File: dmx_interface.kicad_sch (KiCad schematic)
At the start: 12 parts, among them J1 NC3MAAH, J2 NC3FAAH, U1 ST485E

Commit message: mcu pinouts and extras
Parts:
- *C3, *C4: footprint (none) -> Capacitor_SMD:C_0603_1608Metric_Pad1.08x0.95mm_HandSolder
- JP1: footprint (none) -> Jumper:SolderJumper-2_P1.3mm_Bridged_RoundedPad1.0x1.5mm
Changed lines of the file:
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@@
 			)
 		)
-		(property "Footprint" ""
+		(property "Footprint" "Capacitor_SMD:C_0603_1608Metric_Pad1.08x0.95mm_HandSolder"
 			(at 162.2552 90.17 0)
 			(effects
@@
 			)
 		)
-		(property "Footprint" ""
+		(property "Footprint" "Jumper:SolderJumper-2_P1.3mm_Bridged_RoundedPad1.0x1.5mm"
 			(at 66.04 72.39 0)
 			(effects
@@
 			)
 		)
-		(property "Footprint" ""
+		(property "Footprint" "Capacitor_SMD:C_0603_1608Metric_Pad1.08x0.95mm_HandSolder"
 			(at 169.8752 67.31 0)
 			(effects

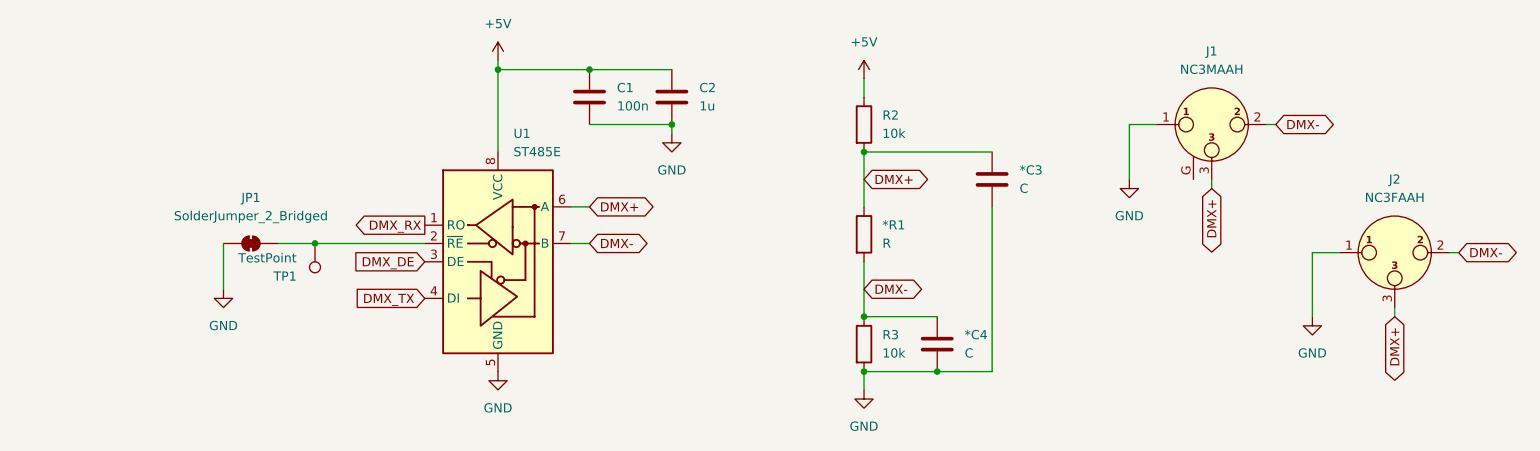
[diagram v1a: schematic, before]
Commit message: add probe headers
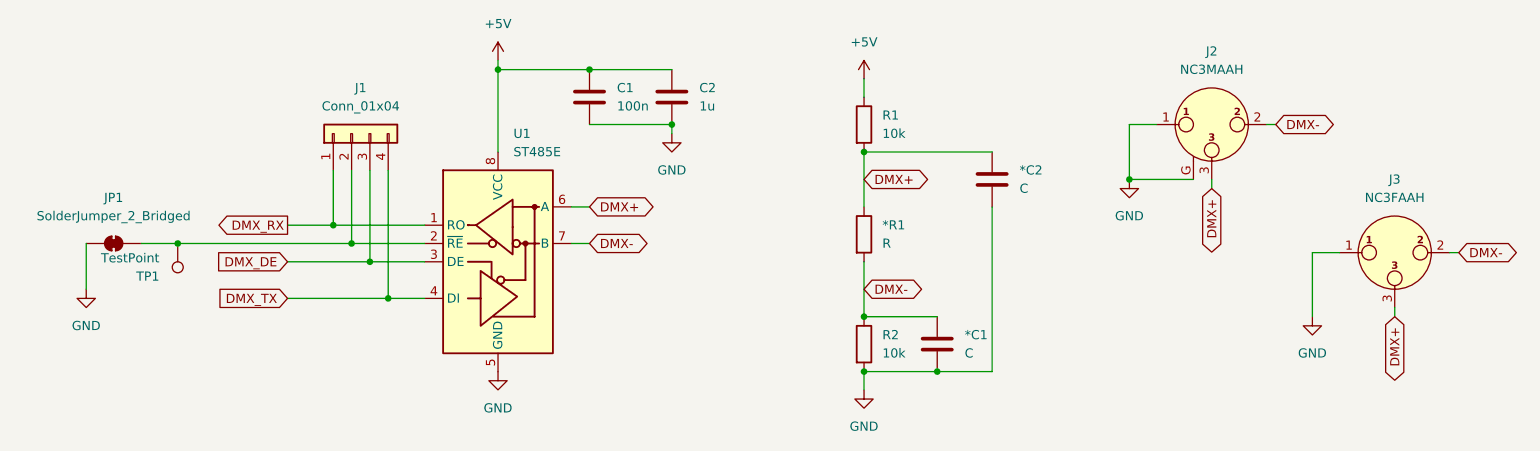
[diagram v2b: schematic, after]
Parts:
- added J1: Conn_01x04, Connector_PinHeader_2.54mm:PinHeader_1x04_P2.54mm_Vertical, symbol Connector_Generic:Conn_01x04
- *R1: footprint Resistor_SMD:R_0201_0603Metric_Pad0.64x0.40mm_HandSolder -> Resistor_SMD:R_0603_1608Metric_Pad0.98x0.95mm_HandSolder
- renumbered *C4 to *C1, *C3 to *C2, J1 to J2, J2 to J3, R2 to R1, R3 to R2
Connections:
- net DMX_DE: now also J1.3 (Pin_3)
- net DMX_RX: now also J1.1 (Pin_1)
- net DMX_TX: now also J1.4 (Pin_4)
- net GND: now also J2.G
- net at JP1.2 (B), TP1.1, U1.2 (~{RE}): now also J1.2 (Pin_2)
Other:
- moved on the sheet: JP1, TP1

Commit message: partial layout
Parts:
- removed TP1: TestPoint, Connector_PinHeader_2.54mm:PinHeader_1x01_P2.54mm_Vertical, symbol Connector:TestPoint
- renumbered *C1 to C3, *C2 to C4, *R1 to R2, R2 to R3
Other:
- moved on the sheet: JP1
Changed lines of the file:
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@@
-	)
-	(junction
-		(at 55.88 72.39)
-		(diameter 0)
-		(color 0 0 0 0)
 	)
 	(junction
@@
 	(wire
 		(pts
+			(xy 43.18 72.39) (xy 43.18 78.74)
+		)
+		(stroke
+			(width 0)
+			(type default)
+		)
+	)
+	(wire
+		(pts
 			(xy 80.01 62.23) (xy 80.01 72.39)
 		)
@@
 	(wire
 		(pts
-			(xy 43.18 78.74) (xy 43.18 72.39)
-		)
-		(stroke
-			(width 0)
-			(type default)
-		)
-	)
-	(wire
-		(pts
 			(xy 151.13 74.93) (xy 151.13 82.55)
 		)
@@
 	(wire
 		(pts
+			(xy 48.26 72.39) (xy 43.18 72.39)
+		)
+		(stroke
+			(width 0)
+			(type default)
+		)
+	)
+	(wire
+		(pts
 			(xy 191.77 55.88) (xy 187.96 55.88)
 		)
@@
 		(pts
 			(xy 151.13 90.17) (xy 161.29 90.17)
-		)
-		(stroke
-			(width 0)
-			(type default)
-		)
-	)
-	(wire
-		(pts
-			(xy 50.8 72.39) (xy 55.88 72.39)
 		)
 		(stroke
@@
 		(dnp no)
 		(fields_autoplaced yes)
-		(property "Reference" "*C1"
+		(property "Reference" "C3"
 			(at 165.1 85.0899 0)
 			(effects
@@
 			(project "dmxdude"
 				(path "/bd7590c0-6a37-4bf0-a9f2-f26180744ceb/b97b4747-94eb-4c44-b864-2ea799fdae76"
-					(reference "*C1")
+					(reference "C3")
 					(unit 1)
 				)
@@
 	)
 	(symbol
-		(lib_id "Connector:TestPoint")
-		(at 55.88 72.39 180)
-		(unit 1)
-		(exclude_from_sim no)
-		(in_bom no)
-		(on_board yes)
-		(dnp no)
-		(property "Reference" "TP1"
-			(at 53.34 76.9621 0)
-			(effects
-				(font
-					(size 1.27 1.27)
-				)
-				(justify left)
-			)
-		)
-		(property "Value" "TestPoint"
-			(at 53.34 74.4221 0)
-			(effects
-				(font
-					(size 1.27 1.27)
-				)
-				(justify left)
-			)
-		)
-		(property "Footprint" "Connector_PinHeader_2.54mm:PinHeader_1x01_P2.54mm_Vertical"
-			(at 50.8 72.39 0)
-			(effects
-				(font
-					(size 1.27 1.27)
-				)
-				(hide yes)
-			)
-		)
-		(property "Datasheet" "~"
-			(at 50.8 72.39 0)
-			(effects
-				(font
-					(size 1.27 1.27)
-				)
-				(hide yes)
-			)
-		)
-		(property "Description" "test point"
-			(at 55.88 72.39 0)
-			(effects
-				(font
-					(size 1.27 1.27)
-				)
-				(hide yes)
-			)
-		)
-		(pin "1"
-		)
-		(instances
-			(project "dmxdude"
-				(path "/bd7590c0-6a37-4bf0-a9f2-f26180744ceb/b97b4747-94eb-4c44-b864-2ea799fdae76"
-					(reference "TP1")
-					(unit 1)
-				)
-			)
-		)
-	)
-	(symbol
 		(lib_id "Device:R")
 		(at 151.13 86.36 0)
@@
 		(dnp no)
 		(fields_autoplaced yes)
-		(property "Reference" "R2"
+		(property "Reference" "R3"
 			(at 153.67 85.0899 0)
 			(effects
@@
 			(project "dmxdude"
 				(path "/bd7590c0-6a37-4bf0-a9f2-f26180744ceb/b97b4747-94eb-4c44-b864-2ea799fdae76"
-					(reference "R2")
+					(reference "R3")
 					(unit 1)
 				)
@@
 		(dnp no)
 		(fields_autoplaced yes)
-		(property "Reference" "*R1"
+		(property "Reference" "R2"
 			(at 153.67 69.8499 0)
 			(effects
@@
 			(project "dmxdude"
 				(path "/bd7590c0-6a37-4bf0-a9f2-f26180744ceb/b97b4747-94eb-4c44-b864-2ea799fdae76"
-					(reference "*R1")
+					(reference "R2")
 					(unit 1)
 				)
@@
 	(symbol
 		(lib_id "Jumper:SolderJumper_2_Bridged")
-		(at 46.99 72.39 0)
+		(at 52.07 72.39 0)
 		(unit 1)
 		(exclude_from_sim no)
@@
 		(fields_autoplaced yes)
 		(property "Reference" "JP1"
-			(at 46.99 66.04 0)
+			(at 52.07 66.04 0)
 			(effects
 				(font
@@
 		)
 		(property "Value" "SolderJumper_2_Bridged"
-			(at 46.99 68.58 0)
+			(at 52.07 68.58 0)
 			(effects
 				(font
@@
 		)
 		(property "Footprint" "Jumper:SolderJumper-2_P1.3mm_Bridged_RoundedPad1.0x1.5mm"
-			(at 46.99 72.39 0)
+			(at 52.07 72.39 0)
 			(effects
 				(font
@@
 		)
 		(property "Datasheet" "~"
-			(at 46.99 72.39 0)
+			(at 52.07 72.39 0)
 			(effects
 				(font
@@
 		)
 		(property "Description" "Solder Jumper, 2-pole, closed/bridged"
-			(at 46.99 72.39 0)
+			(at 52.07 72.39 0)
 			(effects
 				(font
@@
 		(dnp no)
 		(fields_autoplaced yes)
-		(property "Reference" "*C2"
+		(property "Reference" "C4"
 			(at 172.72 62.2299 0)
 			(effects
@@
 			(project "dmxdude"
 				(path "/bd7590c0-6a37-4bf0-a9f2-f26180744ceb/b97b4747-94eb-4c44-b864-2ea799fdae76"
-					(reference "*C2")
+					(reference "C4")
 					(unit 1)
 				)
